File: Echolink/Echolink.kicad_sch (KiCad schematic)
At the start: 43 parts, among them J1 USB_B, J2 AUDIO_PC, J3 AUDIO_TRX, J4 MountHole, J5 CAT, J6 PTT_CW, J7 MountHole, J8 MountHole, J9 MountHole, K11 TIANBO-HJR-4102-L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

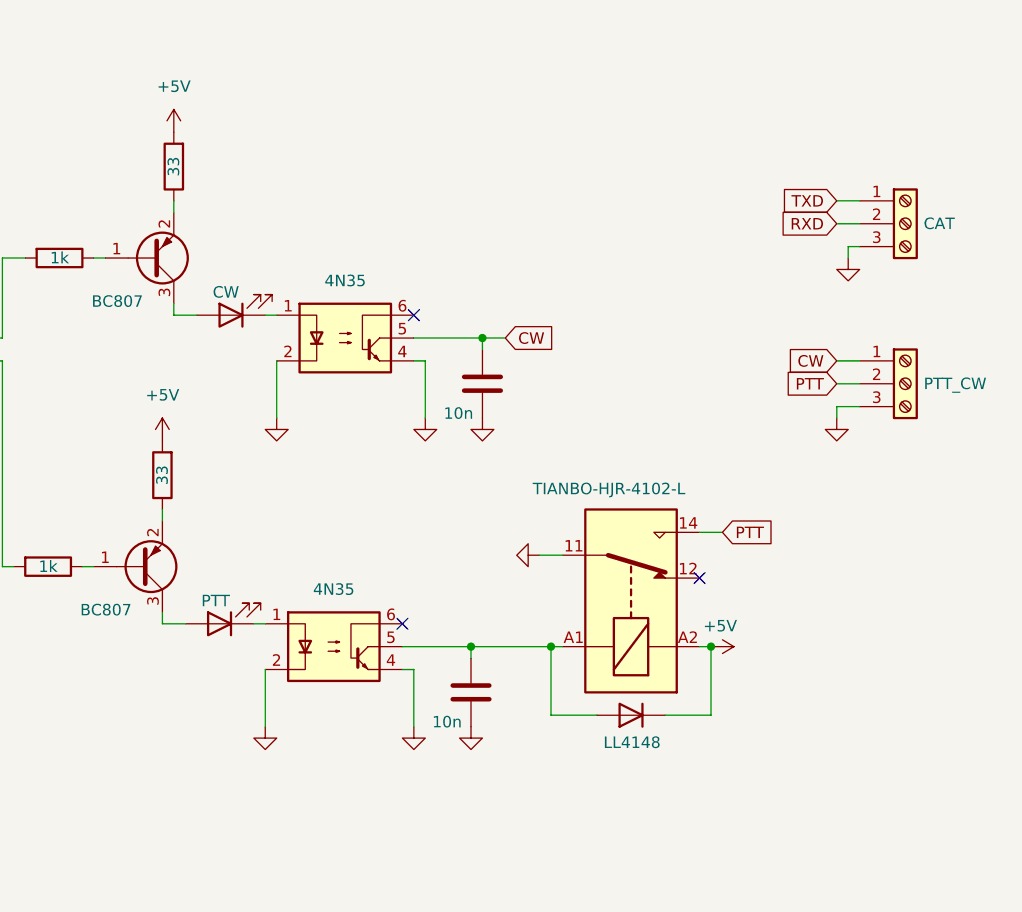
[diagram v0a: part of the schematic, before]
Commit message: change optotransistor, add some pics
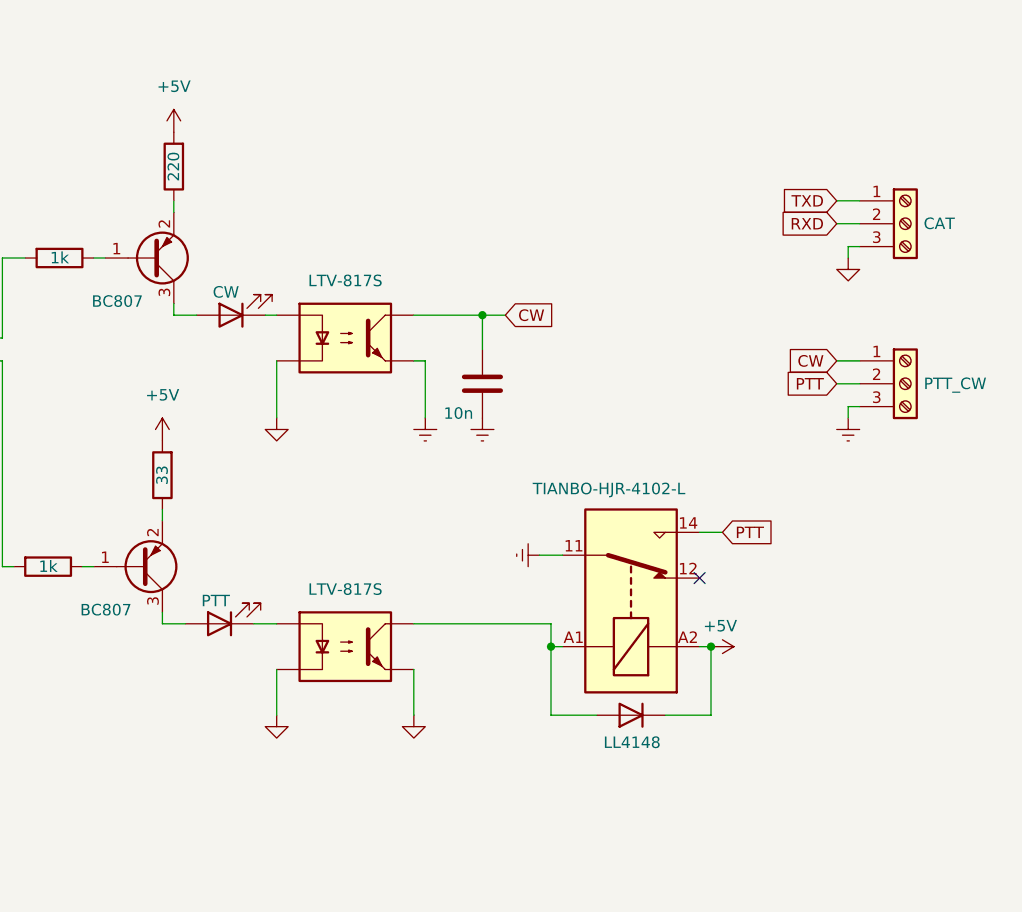
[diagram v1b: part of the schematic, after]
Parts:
- removed C6: 10n, Capacitor_SMD:C_1206_3216Metric, symbol Device:C
- removed U3, U4: 4N35, Package_DIP:DIP-6_W7.62mm, symbol Isolator:4N35
- added U5, U6: LTV-817S, Package_DIP:SMDIP-4_W9.53mm, symbol Isolator:LTV-817S
- R7: value 33 -> 220
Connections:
- net CW: now also U6.4
- net GND: now also U5.2, U5.3, U6.2; no longer C5.2, J6.3 (Pin_3), K11.11
- net at D3.2 (A), K11.A1: now also U5.4
- net at D4.1 (K): now also U5.1
- net at D2.1 (K): now also U6.1
- new net GNDREF: C5.2, J6.3 (Pin_3), K11.11, U6.3
- no-connect marks 8 -> 6
